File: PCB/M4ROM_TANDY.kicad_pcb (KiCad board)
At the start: 2 copper layers, 38 x 16.6 mm, 7 parts, among them J1 Tandy_100_102_200_option_rom, J2 4ROM_prog_female, SW1 CUS-14TB, U1 29F010

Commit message: pcb polish
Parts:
- SW1: footprint 000_LOCAL:SW_SP4T_CUS-14B -> 000_LOCAL:SW_SP4T_CUS-14B - PTH
- moved C1 0.15 mm to (133.0, 100.4)
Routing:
- net /D3: track 16.6 -> 17.5 mm
- net /D4: track 15.7 -> 14.9 mm
- net /D7: track 10.9 -> 10.2 mm, vias 2 -> 1

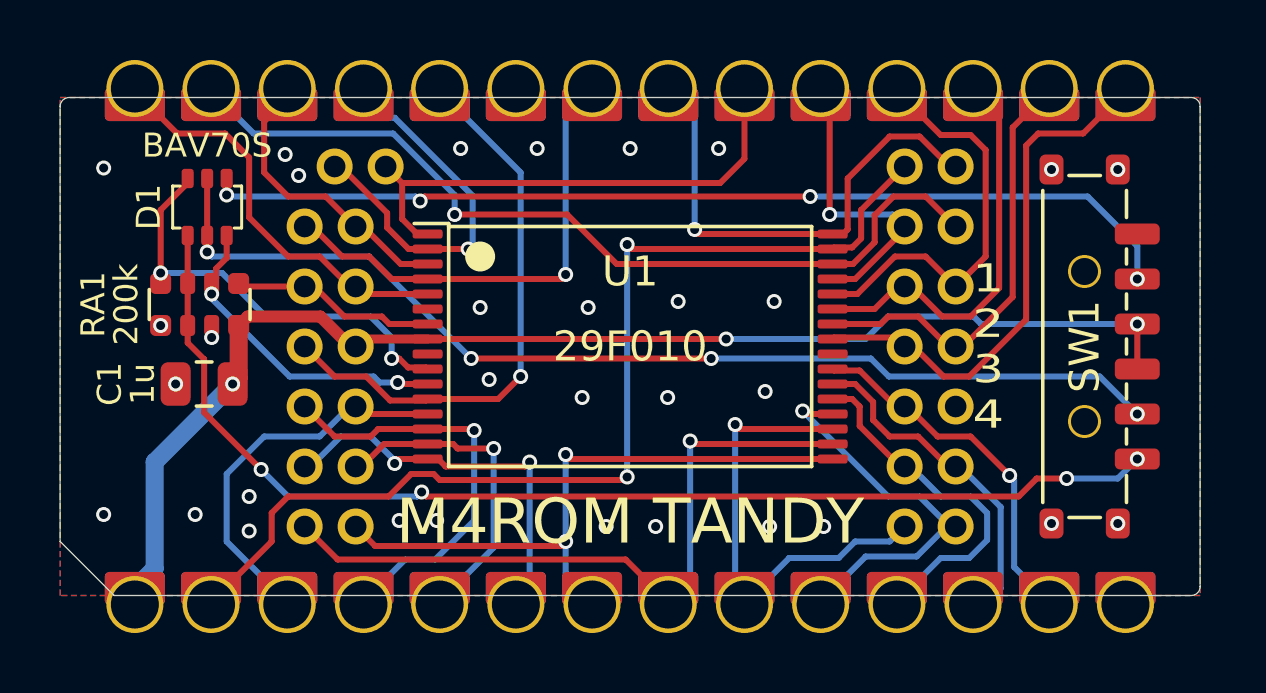
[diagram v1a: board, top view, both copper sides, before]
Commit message: improve some teardrops
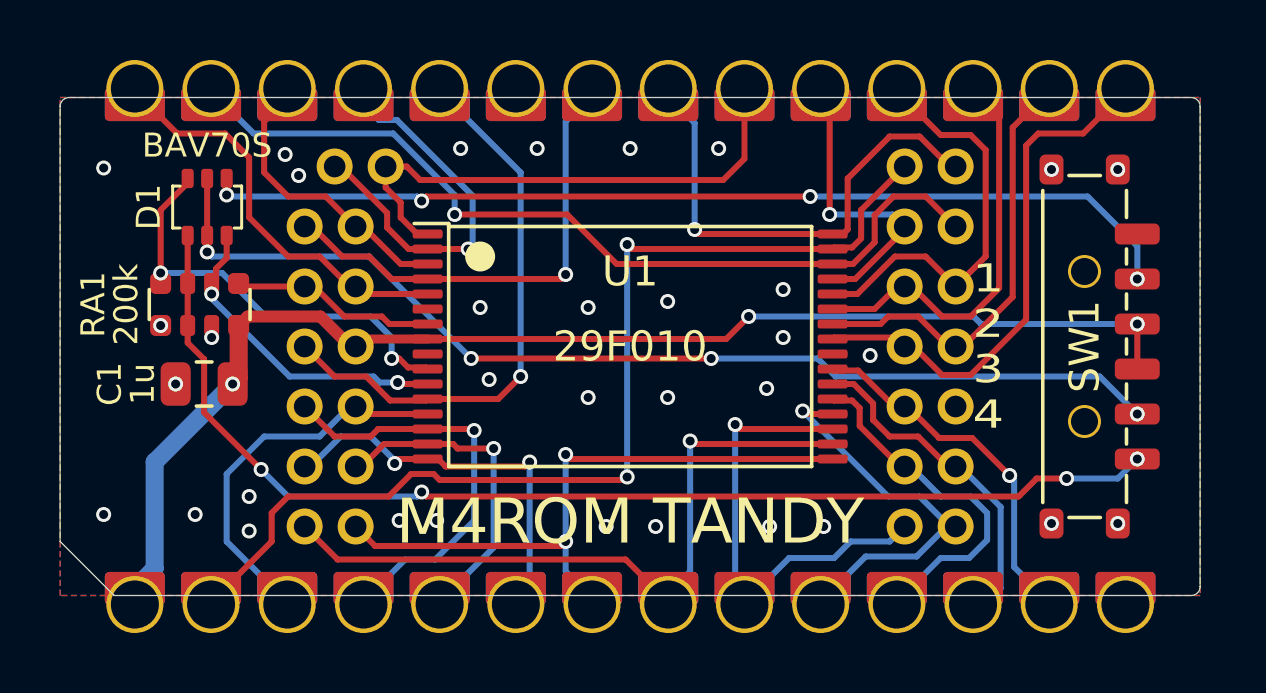
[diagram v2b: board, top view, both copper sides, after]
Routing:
- net /A11: track 16.6 -> 17.3 mm
- net /A4: track 13.0 -> 13.5 mm
- net GND: vias 32 -> 34
